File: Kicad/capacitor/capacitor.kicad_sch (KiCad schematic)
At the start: 141 parts, among them K1 Capacitor

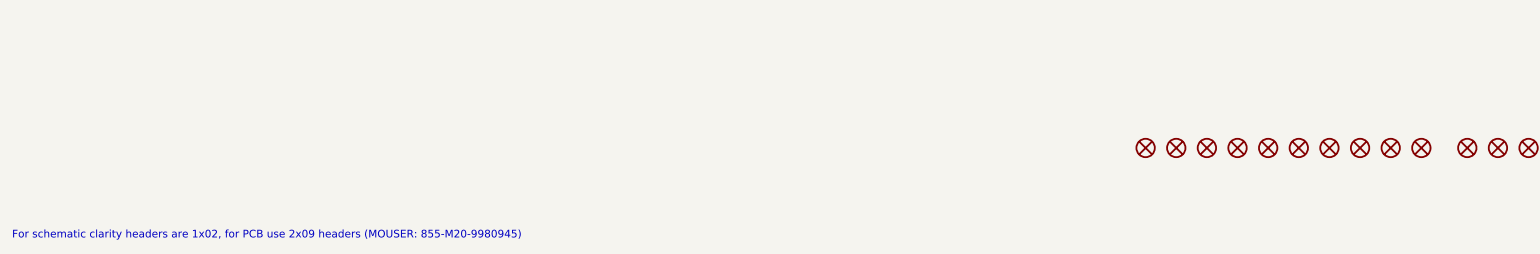
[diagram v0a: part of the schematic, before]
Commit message: Update capacitor.kicad_sch
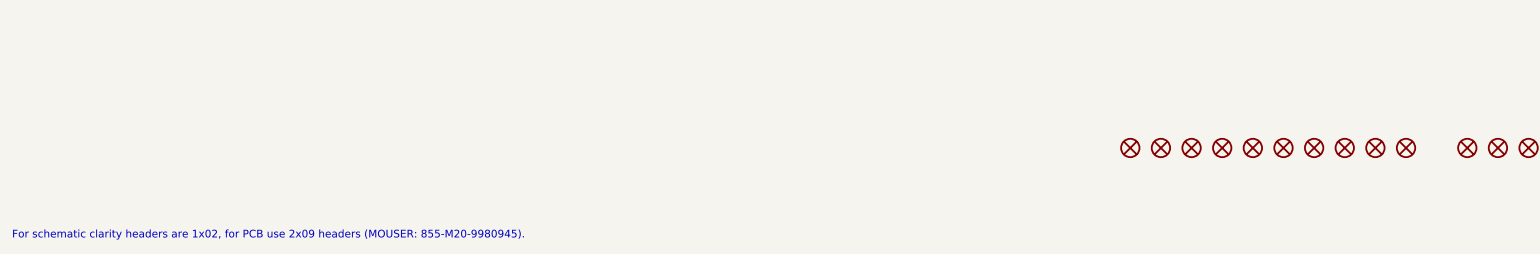
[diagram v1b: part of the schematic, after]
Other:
- note added: "For schematic clarity headers are 1x02, for PCB use 2x09 headers (MOUSER: 855-M20-9980945)."
- note removed: "For schematic clarity headers are 1x02, for PCB use 2x09 headers (MOUSER: 855-M20-9980945)"

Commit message: Update capacitor.kicad_sch
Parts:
- C1, C2, C3, C4, C5, C6, C7, C8, C9: MOUSER 80-C1206X106J3R -> (none); Mouser (none) -> 80-C1206X106J3R
- C10, C11, C12, C13, C14, C15, C16, C17, C18: MOUSER 581-12063C105JAT2A -> (none); Mouser (none) -> 581-12063C105JAT2A
- C19, C20, C21, C22, C23, C24, C25, C26, C27: MOUSER 581-12063C104JAT2A -> (none); Mouser (none) -> 581-12063C104JAT2A
- C28, C29, C30, C31, C32, C33, C34, C35, C36: MOUSER 581-12063C103JAT2A -> (none); Mouser (none) -> 581-12063C103JAT2A
- C37, C38, C39, C40, C41, C42, C43, C44, C45: MOUSER 581-12063C102JAT2A -> (none); Mouser (none) -> 581-12063C102JAT2A
- C46, C47, C48, C49, C50, C51, C52, C53, C54: MOUSER 581-12061C101JAT2A -> (none); Mouser (none) -> 581-12061C101JAT2A
- C55, C56, C57, C58, C59, C60, C61, C62, C63: MOUSER 80-C1206C100J5GACTU -> (none); Mouser (none) -> 80-C1206C100J5GACTU
- H12, H3, H9: MOUSER 534-9056 -> (none); Mouser (none) -> 534-9056
- H6: Mouser (none) -> 534-9056
- JP1, JP10, JP11, JP12, JP13, JP14, JP15, JP16, JP17, JP18, JP19, JP2, JP20, JP21, JP22, JP23, JP24, JP25, JP26, JP27, JP28, JP29, JP3, JP30, JP31, JP32, JP33, JP34, JP35, JP36, JP37, JP38, JP39, JP4, JP40, JP41, JP42, JP43, JP44, JP45, JP46, JP47, JP48, JP49, JP5, JP50, JP51, JP52, JP53, JP54, JP55, JP56, JP57, JP58, JP59, JP6, JP60, JP61, JP62, JP63, JP7, JP8, JP9: MOUSER 855-M20-999024 -> (none); Mouser (none) -> 855-M20-999024
- JP64, JP65, JP66, JP67, JP68, JP69, JP70, JP71, JP72, JP73: MOUSER 855-M7682 -> (none); Mouser (none) -> 855-M7682
- K1: MOUSER 55-M20-9990245 -> (none); Mouser (none) -> 55-M20-9990245
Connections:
- net at C43.1: now also JP47.2; no longer JP43.2
- net at C5.1: now also JP29.2; no longer JP5.2
- net at C30.1: now also JP18.2; no longer JP30.2
- net at JP36.2: now also C6.1; no longer C36.1
- net at C18.1: now also JP58.2; no longer JP18.2
- net at JP60.2: now also C36.1; no longer C60.1
- net at C22.1: now also JP24.2; no longer JP22.2
- net at C61.1: now also JP49.2; no longer JP61.2
- net at C23.1: now also JP31.2; no longer JP23.2
- net at JP48.2: now also C52.1; no longer C48.1
- net at JP45.2: now also C25.1; no longer C45.1
- net at C19.1: now also JP3.2; no longer JP19.2
- net at C34.1: now also JP46.2; no longer JP34.2
- net at C12.1: now also JP16.2; no longer JP12.2
- net at C47.1: now also JP13.2; no longer JP47.2
- net at C62.1: now also JP56.2; no longer JP62.2
- net at JP7.2: now also C55.1; no longer C7.1
- net at C33.1: now also JP39.2; no longer JP33.2
- net at C59.1: now also JP35.2; no longer JP59.2
- net at JP4.2: now also C28.1; no longer C4.1
- net at C31.1: now also JP25.2; no longer JP31.2
- net at JP52.2: now also C26.1; no longer C52.1
- net at C58.1: now also JP28.2; no longer JP58.2
- net at JP55.2: now also C53.1; no longer C55.1
- net at JP44.2: now also C16.1; no longer C44.1
- net at C15.1: now also JP37.2; no longer JP15.2
- net at C38.1: now also JP12.2; no longer JP38.2
- net at JP8.2: now also C2.1; no longer C8.1
- net at C40.1: now also JP26.2; no longer JP40.2
- net at C42.1: now also JP40.2; no longer JP42.2
- net at C20.1: now also JP10.2; no longer JP20.2
- net at JP50.2: now also C8.1; no longer C50.1
- net at JP51.2: now also C17.1; no longer C51.1
- net at C13.1: now also JP23.2; no longer JP13.2
- net at C9.1: now also JP57.2; no longer JP9.2
- net at JP53.2: now also C35.1; no longer C53.1
- net at C46.1: now also JP6.2; no longer JP46.2
- net at C49.1: now also JP27.2; no longer JP49.2
- net at C29.1: now also JP11.2; no longer JP29.2
- net at C54.1: now also JP62.2; no longer JP54.2
- net at C21.1: now also JP17.2; no longer JP21.2
- net at C11.1: now also JP9.2; no longer JP11.2
- net at C56.1: now also JP14.2; no longer JP56.2
- net at C27.1: now also JP59.2; no longer JP27.2
- net at JP41.2: now also C51.1; no longer C41.1
- net at C57.1: now also JP21.2; no longer JP57.2
- net at C14.1: now also JP30.2; no longer JP14.2
- net at C37.1: now also JP5.2; no longer JP37.2
- net at C24.1: now also JP38.2; no longer JP24.2
- net at C39.1: now also JP19.2; no longer JP39.2
- net at JP2.2: now also C10.1; no longer C2.1
- net at C3.1: now also JP15.2; no longer JP3.2
- new net: C44.1, JP54.2
- new net: C45.1, JP61.2
- new net: C4.1, JP22.2
- new net: C48.1, JP20.2
- new net: C41.1, JP33.2
- new net: C7.1, JP43.2
- new net: C60.1, JP42.2
- new net: C50.1, JP34.2

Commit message: Update Capacitor
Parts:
- renumbered H3 to H1, H6 to H2, H9 to H3, H12 to H4, JP2 to JP10, JP9 to JP11, JP16 to JP12, JP23 to JP13, JP30 to JP14, JP37 to JP15, JP44 to JP16, JP51 to JP17, JP58 to JP18, JP3 to JP19, JP8 to JP2, JP10 to JP20, JP17 to JP21, JP24 to JP22, JP31 to JP23, JP38 to JP24, JP45 to JP25, JP52 to JP26, JP59 to JP27, JP4 to JP28, JP11 to JP29, JP15 to JP3, JP18 to JP30, JP25 to JP31, JP39 to JP33, JP46 to JP34, JP53 to JP35, JP60 to JP36, JP5 to JP37, JP12 to JP38, JP19 to JP39, JP22 to JP4, JP26 to JP40, JP33 to JP41, JP40 to JP42, JP47 to JP43, JP54 to JP44, JP61 to JP45, JP6 to JP46, JP13 to JP47, JP20 to JP48, JP27 to JP49, JP29 to JP5, JP34 to JP50, JP41 to JP51, JP48 to JP52, JP55 to JP53, JP62 to JP54, JP7 to JP55, JP14 to JP56, JP21 to JP57, JP28 to JP58, JP35 to JP59, JP36 to JP6, JP42 to JP60, JP49 to JP61, JP56 to JP62, JP43 to JP7, JP50 to JP8, JP57 to JP9

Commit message: Update
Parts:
- C1, C2, C3, C4, C5, C6, C7, C8, C9: footprint tronixio:CAPACITOR-1206 -> tronixio:CAPACITOR-SMD-1206; symbol tronixio:C-1206 -> tronixio:CAPACITOR-1206-10U-5P; Name (none) -> CAPACITOR-1206-10U-5P; Tolerance (none) -> 5%; Voltage (none) -> 50V
- C10, C11, C12, C13, C14, C15, C16, C17, C18: footprint tronixio:CAPACITOR-1206 -> tronixio:CAPACITOR-SMD-1206; symbol tronixio:C-1206 -> tronixio:CAPACITOR-1206-1U-5P; Mouser 581-12063C105JAT2A -> 80-C1206C105J5R; Name (none) -> CAPACITOR-1206-1U-5P; Tolerance (none) -> 5%; Voltage (none) -> 50V
- C19, C20, C21, C22, C23, C24, C25, C26, C27: footprint tronixio:CAPACITOR-1206 -> tronixio:CAPACITOR-SMD-1206; symbol tronixio:C-1206 -> tronixio:CAPACITOR-1206-100N-5P; Mouser 581-12063C104JAT2A -> 80-C1206C104J5R; Name (none) -> CAPACITOR-1206-100N-5P; Tolerance (none) -> 5%; Voltage (none) -> 50V
- C28, C29, C30, C31, C32, C33, C34, C35, C36: footprint tronixio:CAPACITOR-1206 -> tronixio:CAPACITOR-SMD-1206; symbol tronixio:C-1206 -> tronixio:CAPACITOR-1206-10N-5P; Mouser 581-12063C103JAT2A -> 80-C1206C103J5R; Name (none) -> CAPACITOR-1206-10N-5P; Tolerance (none) -> 5%; Voltage (none) -> 50V
- C37, C38, C39, C40, C41, C42, C43, C44, C45: footprint tronixio:CAPACITOR-1206 -> tronixio:CAPACITOR-SMD-1206; symbol tronixio:C-1206 -> tronixio:CAPACITOR-1206-1N-5P; Mouser 581-12063C102JAT2A -> 80-C1206C102J5R; Name (none) -> CAPACITOR-1206-1N-5P; Tolerance (none) -> 5%; Voltage (none) -> 50V
- C46, C47, C48, C49, C50, C51, C52, C53, C54: footprint tronixio:CAPACITOR-1206 -> tronixio:CAPACITOR-SMD-1206; symbol tronixio:C-1206 -> tronixio:CAPACITOR-1206-100P-5P; Mouser 581-12061C101JAT2A -> 80-C1206C101J5G; Name (none) -> CAPACITOR-1206-100P-5P; Tolerance (none) -> 5%; Voltage (none) -> 50V
- C55, C56, C57, C58, C59, C60, C61, C62, C63: footprint tronixio:CAPACITOR-1206 -> tronixio:CAPACITOR-SMD-1206; symbol tronixio:C-1206 -> tronixio:CAPACITOR-1206-10P-5P; Name (none) -> CAPACITOR-1206-10P-5P; Tolerance (none) -> 5%; Voltage (none) -> 50V
- H2: MOUSER 534-9056 -> (none)
- JP1, JP10, JP11, JP12, JP13, JP14, JP15, JP16, JP17, JP18, JP19, JP2, JP20, JP21, JP22, JP23, JP24, JP25, JP26, JP27, JP28, JP29, JP3, JP30, JP31, JP32, JP33, JP34, JP35, JP36, JP37, JP38, JP39, JP4, JP40, JP41, JP42, JP43, JP44, JP45, JP46, JP47, JP48, JP49, JP5, JP50, JP51, JP52, JP53, JP54, JP55, JP56, JP57, JP58, JP59, JP6, JP60, JP61, JP62, JP63, JP7, JP8, JP9: Name (none) -> HARWIN-254-M-1X02-JUMPER-VERTICAL
- K1: Name (none) -> HARWIN-254-M-1X02-VERTICAL

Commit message: Up
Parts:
- removed C11, C12, C13, C14, C15, C16, C17, C18: 1µ, tronixio:CAPACITOR-SMD-1206, symbol tronixio:CAPACITOR-1206-1U-5P
- removed C2, C3, C4, C5, C6, C7, C8, C9: 10µ, tronixio:CAPACITOR-SMD-1206, symbol tronixio:CAPACITOR-1206-10U-5P
- removed C20, C21, C22, C23, C24, C25, C26, C27: 100n, tronixio:CAPACITOR-SMD-1206, symbol tronixio:CAPACITOR-1206-100N-5P
- removed C29, C30, C31, C32, C33, C34, C35, C36: 10n, tronixio:CAPACITOR-SMD-1206, symbol tronixio:CAPACITOR-1206-10N-5P
- removed C38, C39, C40, C41, C42, C43, C44, C45: 1n, tronixio:CAPACITOR-SMD-1206, symbol tronixio:CAPACITOR-1206-1N-5P
- removed C47, C48, C49, C50, C51, C52, C53, C54: 100p, tronixio:CAPACITOR-SMD-1206, symbol tronixio:CAPACITOR-1206-100P-5P
- removed C56, C57, C58, C59, C60, C61, C62, C63: 10p, tronixio:CAPACITOR-SMD-1206, symbol tronixio:CAPACITOR-1206-10P-5P
- added C11, C12, C13, C14, C15, C16, C17, C18: 1µ, tronixio:CAPACITOR-SMD-1206, symbol tronixio:CAPACITOR-1206-1U-5P-X7R
- added C2, C3, C4, C5, C6, C7, C8, C9: 10µ, tronixio:CAPACITOR-SMD-1206, symbol tronixio:CAPACITOR-1206-10U-5P-X7R
- added C20, C21, C22, C23, C24, C25, C26, C27: 100n, tronixio:CAPACITOR-SMD-1206, symbol tronixio:CAPACITOR-1206-100N-5P-X7R
- added C29, C30, C31, C32, C33, C34, C35, C36: 10n, tronixio:CAPACITOR-SMD-1206, symbol tronixio:CAPACITOR-1206-10N-5P-X7R
- added C38, C39, C40, C41, C42, C43, C44, C45: 1n, tronixio:CAPACITOR-SMD-1206, symbol tronixio:CAPACITOR-1206-1N-5P-COG
- added C47, C48, C49, C50, C51, C52, C53, C54: 100p, tronixio:CAPACITOR-SMD-1206, symbol tronixio:CAPACITOR-1206-100P-5P-COG
- added C56, C57, C58, C59, C60, C61, C62, C63: 10p, tronixio:CAPACITOR-SMD-1206, symbol tronixio:CAPACITOR-1206-10P-5P-COG
- C1: symbol tronixio:CAPACITOR-1206-10U-5P -> tronixio:CAPACITOR-1206-10U-5P-X7R; Name CAPACITOR-1206-10U-5P -> (none); Voltage 50V -> 25V
- C10: symbol tronixio:CAPACITOR-1206-1U-5P -> tronixio:CAPACITOR-1206-1U-5P-X7R; Name CAPACITOR-1206-1U-5P -> (none)
- C19: symbol tronixio:CAPACITOR-1206-100N-5P -> tronixio:CAPACITOR-1206-100N-5P-X7R; Name CAPACITOR-1206-100N-5P -> (none)
- C28: symbol tronixio:CAPACITOR-1206-10N-5P -> tronixio:CAPACITOR-1206-10N-5P-X7R; Name CAPACITOR-1206-10N-5P -> (none)
- C37: symbol tronixio:CAPACITOR-1206-1N-5P -> tronixio:CAPACITOR-1206-1N-5P-COG; Mouser 80-C1206C102J5R -> 80-C1206C103JAGECAUT; Name CAPACITOR-1206-1N-5P -> (none); Voltage 50V -> 250V
- C46: symbol tronixio:CAPACITOR-1206-100P-5P -> tronixio:CAPACITOR-1206-100P-5P-COG; Name CAPACITOR-1206-100P-5P -> (none)
- C55: symbol tronixio:CAPACITOR-1206-10P-5P -> tronixio:CAPACITOR-1206-10P-5P-COG; Name CAPACITOR-1206-10P-5P -> (none)
- JP1, JP10, JP11, JP12, JP13, JP14, JP15, JP16, JP17, JP18, JP19, JP2, JP20, JP21, JP22, JP23, JP24, JP25, JP26, JP27, JP28, JP29, JP3, JP30, JP31, JP32, JP33, JP34, JP35, JP36, JP37, JP38, JP39, JP4, JP40, JP41, JP42, JP43, JP44, JP45, JP46, JP47, JP48, JP49, JP5, JP50, JP51, JP52, JP53, JP54, JP55, JP56, JP57, JP58, JP59, JP6, JP60, JP61, JP62, JP63, JP7, JP8, JP9: Name HARWIN-254-M-1X02-JUMPER-VERTICAL -> (none)
- K1: Name HARWIN-254-M-1X02-VERTICAL -> (none)
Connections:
- net at JP16.2: now also C16.1
- net at C1.2, C10.2, C19.2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: now also C11.2, C12.2, C13.2, C14.2, C15.2, C16.2, C17.2, C18.2, C2.2, C20.2, C21.2, C22.2, C23.2, C24.2, C25.2, C26.2, C27.2, C29.2, C3.2, C30.2, C31.2, C32.2, C33.2, C34.2, C35.2, C36.2, C38.2, C39.2, C4.2, C40.2, C41.2, C42.2, C43.2, C44.2, C45.2, C47.2, C48.2, C49.2, C5.2, C50.2, C51.2, C52.2, C53.2, C54.2, C56.2, C57.2, C58.2, C59.2, C6.2, C60.2, C61.2, C62.2, C63.2, C7.2, C8.2, C9.2
- net at JP61.2: now also C61.1
- net at JP40.2: now also C40.1
- net at JP5.2: now also C5.1
- net at JP22.2: now also C22.1
- net at JP62.2: now also C62.1
- net at JP25.2: now also C25.1
- net at JP35.2: now also C35.1
- net at JP52.2: now also C52.1
- net at JP31.2: now also C31.1
- net at JP33.2: now also C33.1
- net at JP56.2: now also C56.1
- net at JP43.2: now also C43.1
- net at JP18.2: now also C18.1
- net at JP12.2: now also C12.1
- net at JP54.2: now also C54.1
- net at JP44.2: now also C44.1
- net at JP42.2: now also C42.1
- net at JP30.2: now also C30.1
- net at JP38.2: now also C38.1
- net at JP34.2: now also C34.1
- net at JP59.2: now also C59.1
- net at JP6.2: now also C6.1
- net at JP23.2: now also C23.1
- net at JP20.2: now also C20.1
- net at JP32.2: now also C32.1
- net at JP9.2: now also C9.1
- net at JP45.2: now also C45.1
- net at JP14.2: now also C14.1
- net at JP27.2: now also C27.1
- net at JP24.2: now also C24.1
- net at JP21.2: now also C21.1
- net at JP17.2: now also C17.1
- net at JP4.2: now also C4.1
- net at JP15.2: now also C15.1
- net at JP13.2: now also C13.1
- net at JP51.2: now also C51.1
- net at JP53.2: now also C53.1
- net at JP47.2: now also C47.1
- net at JP36.2: now also C36.1
- net at JP48.2: now also C48.1
- net at JP29.2: now also C29.1
- net at JP11.2: now also C11.1
- net at JP2.2: now also C2.1
- net at JP41.2: now also C41.1
- net at JP7.2: now also C7.1
- net at JP3.2: now also C3.1
- net at JP57.2: now also C57.1
- net at JP60.2: now also C60.1
- net at JP58.2: now also C58.1
- net at JP39.2: now also C39.1
- net at JP8.2: now also C8.1
- net at JP49.2: now also C49.1
- net at JP63.2: now also C63.1
- net at JP26.2: now also C26.1
- net at JP50.2: now also C50.1
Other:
- moved on the sheet: JP1
